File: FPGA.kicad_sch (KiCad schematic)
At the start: 54 parts, among them U3A LFE5U-25F-8MG285C, U3B LFE5U-25F-8MG285C, U3C LFE5U-25F-8MG285C, U3D LFE5U-25F-8MG285C, U3E LFE5U-25F-8MG285C, U3F LFE5U-25F-8MG285C, U3G LFE5U-25F-8MG285C, U6 W25Q128JVP

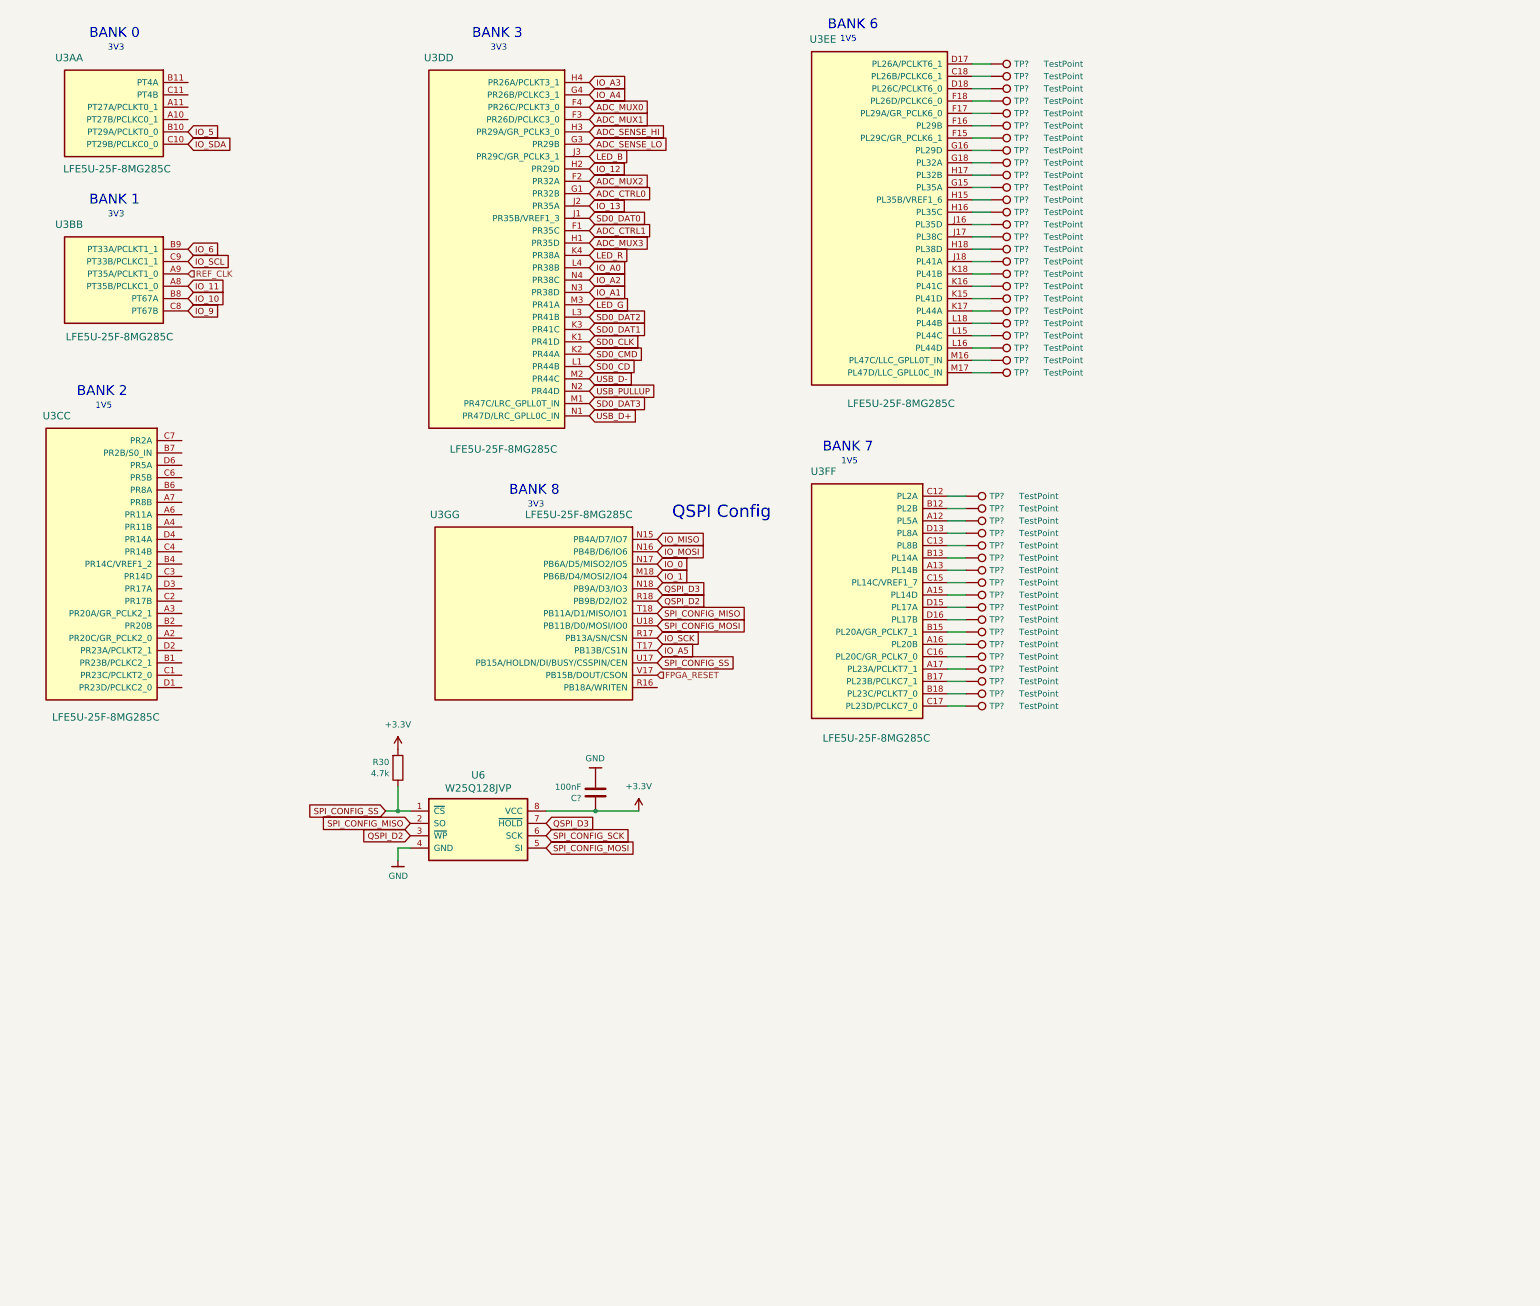
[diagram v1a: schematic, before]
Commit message: complete scheme, add rotary switch, leds and buttons
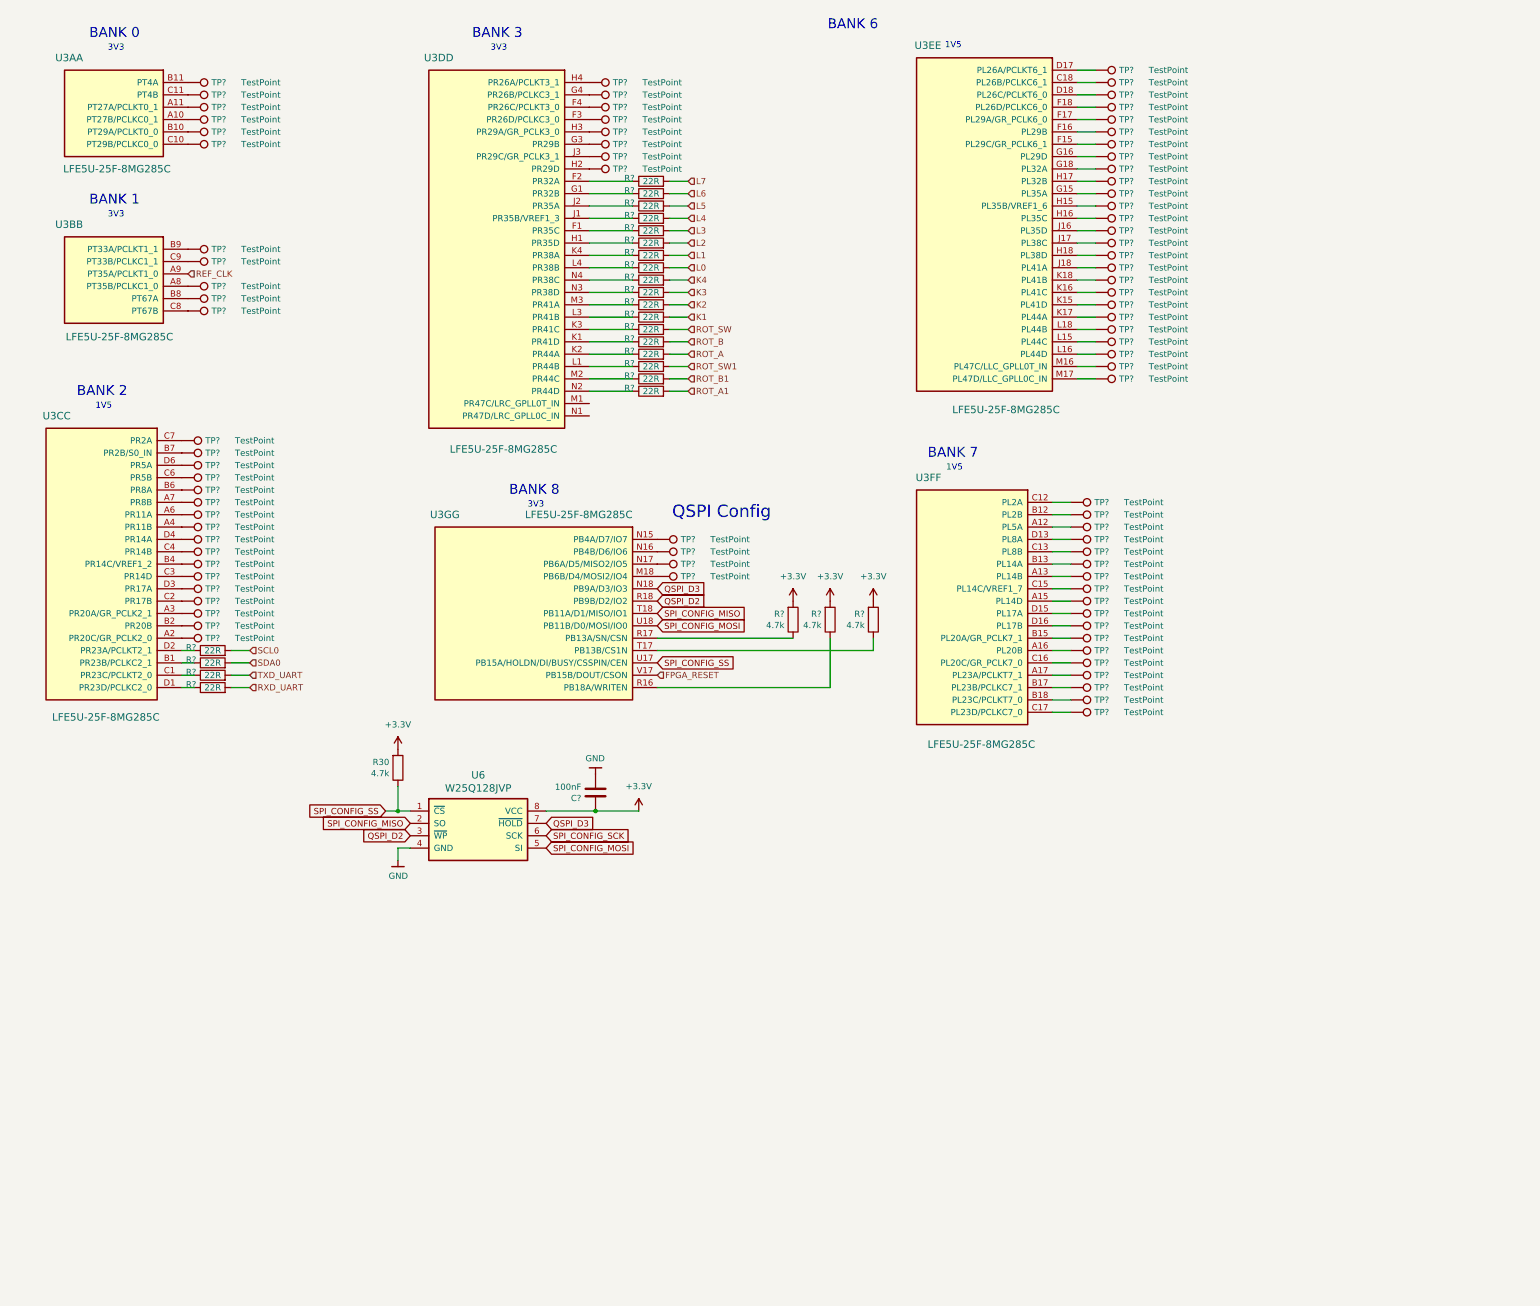
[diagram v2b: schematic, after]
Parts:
- added R? (x3): 4.7k, gkl_dipol:R_0201_0603Metric, symbol Device:R
- added R? (x22): 22R, gkl_dipol:R_0201_0603Metric, symbol Device:R
- added TP? (x40): TestPoint, symbol Connector:TestPoint
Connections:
- net +3.3V: now also R?.2, R?.2, R?.2
- net at U3A.A10 (PT27B/PCLKC0_1): now also TP?.1
- net at U3A.A11 (PT27A/PCLKT0_1): now also TP?.1
- net at U3A.B11 (PT4A): now also TP?.1
- net at U3A.C11 (PT4B): now also TP?.1
- net at U3C.A2 (PR20C/GR_PCLK2_0): now also TP?.1
- net at U3C.A3 (PR20A/GR_PCLK2_1): now also TP?.1
- net at U3C.A4 (PR11B): now also TP?.1
- net at U3C.A6 (PR11A): now also TP?.1
- net at U3C.A7 (PR8B): now also TP?.1
- net at U3C.B1 (PR23B/PCLKC2_1): now also R?.1
- net at U3C.B2 (PR20B): now also TP?.1
- net at U3C.B4 (PR14C/VREF1_2): now also TP?.1
- net at U3C.B6 (PR8A): now also TP?.1
- net at U3C.B7 (PR2B/S0_IN): now also TP?.1
- net at U3C.C1 (PR23C/PCLKT2_0): now also R?.1
- net at U3C.C2 (PR17B): now also TP?.1
- net at U3C.C3 (PR14D): now also TP?.1
- net at U3C.C4 (PR14B): now also TP?.1
- net at U3C.C6 (PR5B): now also TP?.1
- net at U3C.C7 (PR2A): now also TP?.1
- net at U3C.D1 (PR23D/PCLKC2_0): now also R?.1
- net at U3C.D2 (PR23A/PCLKT2_1): now also R?.1
- net at U3C.D3 (PR17A): now also TP?.1
- net at U3C.D4 (PR14A): now also TP?.1
- net at U3C.D6 (PR5A): now also TP?.1
- net at U3G.R16 (PB18A/WRITEN): now also R?.1
- net ADC_CTRL0: no longer names the net of U3D.G1 (PR32B)
- net ADC_CTRL0: now also R?.1
- net ADC_CTRL1: no longer names the net of U3D.F1 (PR35C)
- net ADC_CTRL1: now also R?.1
- net ADC_MUX0: no longer names the net of U3D.F4 (PR26C/PCLKT3_0)
- net ADC_MUX0: now also TP?.1
- net ADC_MUX1: no longer names the net of U3D.F3 (PR26D/PCLKC3_0)
- net ADC_MUX1: now also TP?.1
- net ADC_MUX2: no longer names the net of U3D.F2 (PR32A)
- net ADC_MUX2: now also R?.1
- net ADC_MUX3: no longer names the net of U3D.H1 (PR35D)
- net ADC_MUX3: now also R?.1
- net ADC_SENSE_HI: no longer names the net of U3D.H3 (PR29A/GR_PCLK3_0)
- net ADC_SENSE_HI: now also TP?.1
- net ADC_SENSE_LO: no longer names the net of U3D.G3 (PR29B)
- net ADC_SENSE_LO: now also TP?.1
- net IO_0: no longer names the net of U3G.N17 (PB6A/D5/MISO2/IO5)
- net IO_0: now also TP?.1
- net IO_1: no longer names the net of U3G.M18 (PB6B/D4/MOSI2/IO4)
- net IO_1: now also TP?.1
- net IO_10: no longer names the net of U3B.B8 (PT67A)
- net IO_10: now also TP?.1
- net IO_11: no longer names the net of U3B.A8 (PT35B/PCLKC1_0)
- net IO_11: now also TP?.1
- net IO_12: no longer names the net of U3D.H2 (PR29D)
- net IO_12: now also TP?.1
- net IO_13: no longer names the net of U3D.J2 (PR35A)
- net IO_13: now also R?.1
- net IO_5: no longer names the net of U3A.B10 (PT29A/PCLKT0_0)
- net IO_5: now also TP?.1
- net IO_6: no longer names the net of U3B.B9 (PT33A/PCLKT1_1)
- net IO_6: now also TP?.1
- net IO_9: no longer names the net of U3B.C8 (PT67B)
- net IO_9: now also TP?.1
- net IO_A0: no longer names the net of U3D.L4 (PR38B)
- net IO_A0: now also R?.1
- net IO_A1: no longer names the net of U3D.N3 (PR38D)
- net IO_A1: now also R?.1
- net IO_A2: no longer names the net of U3D.N4 (PR38C)
- net IO_A2: now also R?.1
- net IO_A3: no longer names the net of U3D.H4 (PR26A/PCLKT3_1)
- net IO_A3: now also TP?.1
- net IO_A4: no longer names the net of U3D.G4 (PR26B/PCLKC3_1)
- net IO_A4: now also TP?.1
- net IO_A5: no longer names the net of U3G.T17 (PB13B/CS1N)
- net IO_A5: now also R?.1
- net IO_MISO: no longer names the net of U3G.N15 (PB4A/D7/IO7)
- net IO_MISO: now also TP?.1
- net IO_MOSI: no longer names the net of U3G.N16 (PB4B/D6/IO6)
- net IO_MOSI: now also TP?.1
- net IO_SCK: no longer names the net of U3G.R17 (PB13A/SN/CSN)
- net IO_SCK: now also R?.1
- net IO_SCL: no longer names the net of U3B.C9 (PT33B/PCLKC1_1)
- net IO_SCL: now also TP?.1
- net IO_SDA: no longer names the net of U3A.C10 (PT29B/PCLKC0_0)
- net IO_SDA: now also TP?.1
- net LED_B: no longer names the net of U3D.J3 (PR29C/GR_PCLK3_1)
- net LED_B: now also TP?.1
- net LED_G: no longer names the net of U3D.M3 (PR41A)
- net LED_G: now also R?.1
- net LED_R: no longer names the net of U3D.K4 (PR38A)
- net LED_R: now also R?.1
- net SD0_CD: no longer names the net of U3D.L1 (PR44B)
- net SD0_CD: now also R?.1
- net SD0_CLK: no longer names the net of U3D.K1 (PR41D)
- net SD0_CLK: now also R?.1
- net SD0_CMD: no longer names the net of U3D.K2 (PR44A)
- net SD0_CMD: now also R?.1
- net SD0_DAT0: no longer names the net of U3D.J1 (PR35B/VREF1_3)
- net SD0_DAT0: now also R?.1
- net SD0_DAT1: no longer names the net of U3D.K3 (PR41C)
- net SD0_DAT1: now also R?.1
- net SD0_DAT2: no longer names the net of U3D.L3 (PR41B)
- net SD0_DAT2: now also R?.1
- net SD0_DAT3: no longer names the net of U3D.M1 (PR47C/LRC_GPLL0T_IN)
- net USB_D+: no longer names the net of U3D.N1 (PR47D/LRC_GPLL0C_IN)
- net USB_D-: no longer names the net of U3D.M2 (PR44C)
- net USB_D-: now also R?.1
- net USB_PULLUP: no longer names the net of U3D.N2 (PR44D)
- net USB_PULLUP: now also R?.1
- new net K1: R?.2
- new net K2: R?.2
- new net K3: R?.2
- new net K4: R?.2
- new net L0: R?.2
- new net L1: R?.2
- new net L2: R?.2
- new net L3: R?.2
- new net L4: R?.2
- new net L5: R?.2
- new net L6: R?.2
- new net L7: R?.2
- new net ROT_A: R?.2
- new net ROT_A1: R?.2
- new net ROT_B: R?.2
- new net ROT_B1: R?.2
- new net ROT_SW: R?.2
- new net ROT_SW1: R?.2
- new net RXD_UART: R?.2
- new net SCL0: R?.2
- new net SDA0: R?.2
- new net TXD_UART: R?.2
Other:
- moved on the sheet: TP?, U3EE, U3FF

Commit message: start to assign footprint
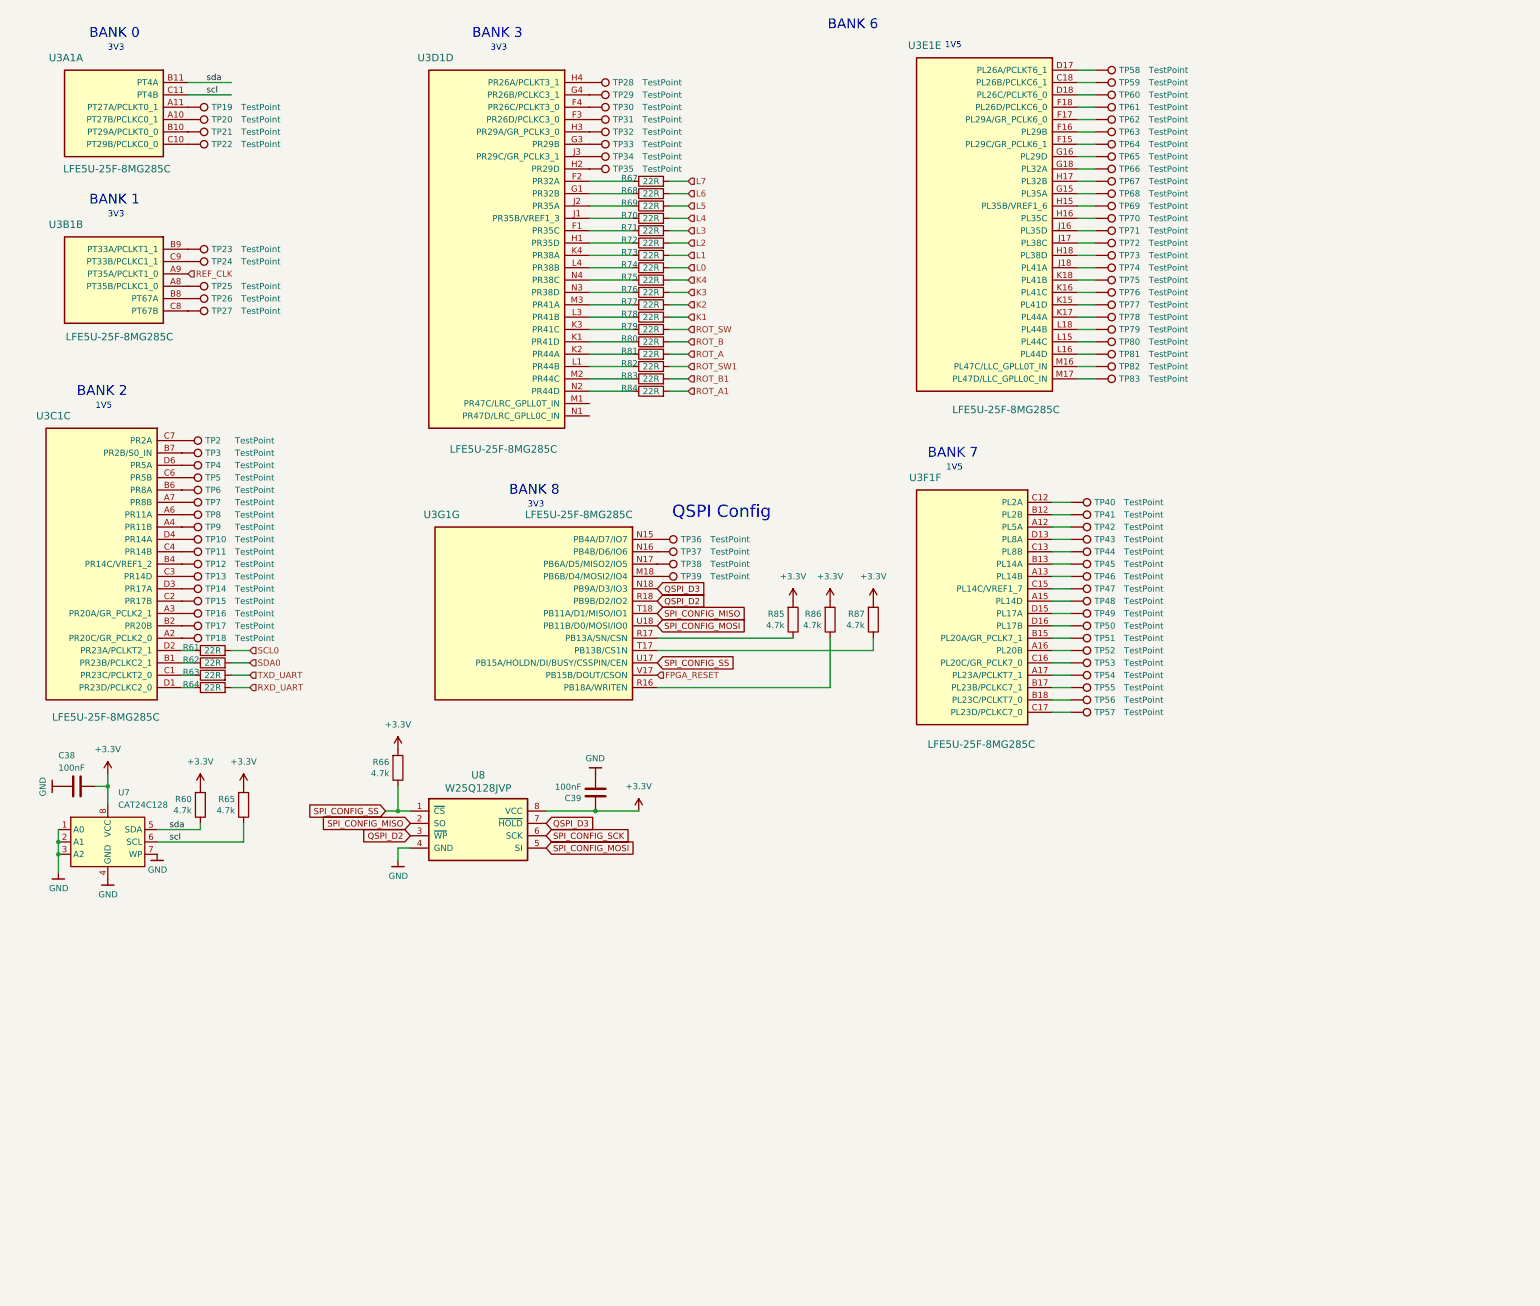
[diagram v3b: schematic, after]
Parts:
- removed TP? (x2): TestPoint, symbol Connector:TestPoint
- added C38: 100nF, Capacitor_SMD:C_0603_1608Metric, symbol Device:C
- added R60, R65: 4.7k, Resistor_SMD:R_0603_1608Metric, symbol Device:R
- added U7: CAT24C128, Package_SO:SOIC-8_3.9x4.9mm_P1.27mm, symbol Memory_EEPROM:CAT24C128
- C39: renamed from C?; footprint gkl_dipol:C_0201_0603Metric -> Capacitor_SMD:C_0603_1608Metric
- R61, R62, R63, R64, R67, R68, R69, R70, R71, R72, R73, R74, R75, R76, R77, R78, R79, R80, R81, R82, R83, R84, R85, R86, R87: renamed from R?; footprint gkl_dipol:R_0201_0603Metric -> Resistor_SMD:R_0603_1608Metric
- R66: renamed from R30; footprint gkl_dipol:R_0201_0603Metric -> Resistor_SMD:R_0603_1608Metric
- TP10, TP11, TP12, TP13, TP14, TP15, TP16, TP17, TP18, TP19, TP2, TP20, TP21, TP22, TP23, TP24, TP25, TP26, TP27, TP28, TP29, TP3, TP30, TP31, TP32, TP33, TP34, TP35, TP36, TP37, TP38, TP39, TP4, TP40, TP41, TP42, TP43, TP44, TP45, TP46, TP47, TP48, TP49, TP5, TP50, TP51, TP52, TP53, TP54, TP55, TP56, TP57, TP58, TP59, TP6, TP60, TP61, TP62, TP63, TP64, TP65, TP66, TP67, TP68, TP69, TP7, TP70, TP71, TP72, TP73, TP74, TP75, TP76, TP77, TP78, TP79, TP8, TP80, TP81, TP82, TP83, TP9: renamed from TP?; footprint (none) -> TestPoint:TestPoint_THTPad_D1.5mm_Drill0.7mm; now left out of the parts list
- renumbered U3A to U3A1, U3B to U3B1, U3C to U3C1, U3D to U3D1, U3E to U3E1, U3F to U3F1, U3G to U3G1, U6 to U8
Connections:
- net +3.3V: now also C38.1, R60.2, R65.2, U7.8 (VCC)
- net GND: now also C38.2, U7.1 (A0), U7.2 (A1), U7.3 (A2), U7.4 (GND), U7.7 (WP)
- net sda: now reaches U3A1.B11 (PT4A)
- net sda: now also R60.1, U7.5 (SDA)
- net scl: now reaches U3A1.C11 (PT4B)
- net scl: now also R65.1, U7.6 (SCL)
